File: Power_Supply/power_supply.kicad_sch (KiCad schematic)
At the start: 14 parts, among them J3 Conn_ARM_SWD_TagConnect, J6 Conn_01x04_Pin, SW1 SW_Push, U1 STM32F401RBTx, Y1 26MHz

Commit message: Updated Schematic and VIM878
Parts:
- removed J3: Conn_ARM_SWD_TagConnect, Connector:Tag-Connect_TC2030-IDC-NL_2x03_P1.27mm_Vertical, symbol Connector:Conn_ARM_SWD_TagConnect_TC2030-NL
- removed J6: Conn_01x04_Pin, symbol Connector:Conn_01x04_Pin
- removed JP1: Jumper_2_Open, TestPoint:TestPoint_Bridge_Pitch2.54mm_Drill0.7mm, symbol Jumper:Jumper_2_Open
- removed R1: 17K, symbol Device:R
- removed R6, R7, R8: 22, symbol Device:R
- added H1, H2, H3, H4: MountingHole, MountingHole:MountingHole_2.1mm, symbol Mechanical:MountingHole
- added H5, H6, H7, H8: MountingHole, MountingHole:MountingHole_3.2mm_M3, symbol Mechanical:MountingHole
- added J3: Conn_01x05_Pin, Connector_JST:JST_EH_B5B-EH-A_1x05_P2.50mm_Vertical, symbol Connector:Conn_01x05_Pin
- added J6: Conn_01x04_Socket, Connector_JST:JST_EH_B4B-EH-A_1x04_P2.50mm_Vertical, symbol Connector:Conn_01x04_Socket
- C11: footprint (none) -> Capacitor_SMD:C_0603_1608Metric
- C12: footprint (none) -> Capacitor_SMD:C_0402_1005Metric
- C14, C15: value 4pF -> 16pF; footprint (none) -> Capacitor_SMD:C_0402_1005Metric
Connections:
- net GND: now also U1.60 (BOOT0), J3.5 (Pin_5), J6.4 (Pin_4)
- net SCL: now also J6.3 (Pin_3)
- net SDA: now also J6.2 (Pin_2)
- net SWCLCK: now also J3.2 (Pin_2)
- net SWDIO: now also J3.3 (Pin_3)
- net SWO: now also J3.4 (Pin_4)
- net VDD: now also J3.1 (Pin_1), J6.1 (Pin_1); no longer U1.1 (VBAT), U1.19 (VDD), U1.32 (VDD), U1.48 (VDD), U1.64 (VDD)
- net SWD_RST: no longer names the net of C12.1, SW1.2, U1.7 (NRST)
- new net +3.3V: U1.1 (VBAT), U1.19 (VDD), U1.32 (VDD), U1.48 (VDD), U1.64 (VDD)

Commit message: Kicad model updated.
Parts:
- removed H7, H8: MountingHole, MountingHole:MountingHole_3.2mm_M3, symbol Mechanical:MountingHole
- J6: footprint Connector_JST:JST_EH_B4B-EH-A_1x04_P2.50mm_Vertical -> Connector_PinSocket_2.54mm:PinSocket_1x04_P2.54mm_Vertical
- Y1: footprint (none) -> Crystal:Crystal_SMD_ECS_CSM3X-2Pin_7.6x4.1mm
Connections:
- net VDD is gone; now on net +3.3V: J3.1 (Pin_1), J6.1 (Pin_1), U1.13 (VREF+)
- net Crystal_out: now reaches C15.2, U1.6 (PH1), Y1.1
- net Crystal_in: now reaches C14.2, U1.5 (PH0), Y1.2
- net V_Cap: now reaches C11.1, U1.30 (VCAP1)
- net Nrst: now reaches C12.1, SW1.2, U1.7 (NRST)
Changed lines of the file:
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@@
+    (stroke (width 0) (type default))
+  )
+  (wire (pts (xy 115.824 68.326) (xy 126.492 68.326))
     (stroke (width 0) (type default))
   )
@@
     (stroke (width 0) (type default))
   )
+  (wire (pts (xy 138.938 45.72) (xy 139.192 45.72))
+    (stroke (width 0) (type default))
+  )
   (wire (pts (xy 146.812 45.72) (xy 146.812 48.006))
     (stroke (width 0) (type default))
@@
     (stroke (width 0) (type default))
   )
-  (wire (pts (xy 139.192 42.926) (xy 139.192 45.72))
+  (wire (pts (xy 138.938 34.544) (xy 138.938 45.72))
     (stroke (width 0) (type default))
   )
@@
     (stroke (width 0) (type default))
   )
+  (wire (pts (xy 254.762 35.052) (xy 253.746 35.052))
+    (stroke (width 0) (type default))
+  )
   (wire (pts (xy 141.732 139.446) (xy 141.732 141.224))
     (stroke (width 0) (type default))
   )
-  (wire (pts (xy 126.492 68.326) (xy 115.824 68.326))
-    (stroke (width 0) (type default))
-  )
   (wire (pts (xy 141.732 48.006) (xy 141.732 45.72))
     (stroke (width 0) (type default))
@@
     (fill (type none))
   )
-  (rectangle (start 240.792 99.822) (end 283.718 143.002)
+  (rectangle (start 240.792 99.822) (end 283.718 130.556)
     (stroke (width 0) (type default))
     (fill (type none))
@@
   (text "Components\n" (at 52.324 65.786 90)
     (effects (font (size 2 2)) (justify left bottom))
+  )
+  (label "V_Cap" (at 114.3 124.206 0) (fields_autoplaced)
+    (effects (font (size 1.27 1.27)) (justify left bottom))
+  )
+  (label "Crystal_out" (at 116.332 70.866 0) (fields_autoplaced)
+    (effects (font (size 1.27 1.27)) (justify left bottom))
+  )
+  (label "Nrst" (at 117.094 53.086 0) (fields_autoplaced)
+    (effects (font (size 1.27 1.27)) (justify left bottom))
+  )
+  (label "Crystal_in" (at 116.332 68.326 0) (fields_autoplaced)
+    (effects (font (size 1.27 1.27)) (justify left bottom))
   )
   (global_label "SWCLCK" (shape input) (at 253.746 37.592 0) (fields_autoplaced)
@@
     )
   )
-  (global_label "VDD" (shape input) (at 260.604 75.946 180) (fields_autoplaced)
-    (effects (font (size 1.27 1.27)) (justify right))
-    (property "Intersheetrefs" "${INTERSHEET_REFS}" (at 254.0696 75.946 0)
-      (effects (font (size 1.27 1.27)) (justify right) hide)
-    )
-  )
   (global_label "SWDIO" (shape input) (at 253.746 40.132 0) (fields_autoplaced)
     (effects (font (size 1.27 1.27)) (justify left))
@@
     )
   )
-  (global_label "VDD" (shape input) (at 122.682 63.246 180) (fields_autoplaced)
-    (effects (font (size 1.27 1.27)) (justify right))
-    (property "Intersheetrefs" "${INTERSHEET_REFS}" (at 116.1476 63.246 0)
-      (effects (font (size 1.27 1.27)) (justify right) hide)
-    )
-  )
-  (global_label "VDD" (shape input) (at 253.746 35.052 0) (fields_autoplaced)
-    (effects (font (size 1.27 1.27)) (justify left))
-    (property "Intersheetrefs" "${INTERSHEET_REFS}" (at 260.2804 35.052 0)
-      (effects (font (size 1.27 1.27)) (justify left) hide)
-    )
-  )
   (global_label "SWCLCK" (shape input) (at 159.385 88.519 0) (fields_autoplaced)
     (effects (font (size 1.27 1.27)) (justify left))
@@
     )
   )
-  (symbol (lib_id "Mechanical:MountingHole") (at 244.348 133.858 0) (unit 1)
-    (in_bom yes) (on_board yes) (dnp no) (fields_autoplaced)
-    (property "Reference" "H7" (at 246.888 133.223 0)
-      (effects (font (size 1.27 1.27)) (justify left))
-    )
-    (property "Value" "MountingHole" (at 246.888 135.763 0)
-      (effects (font (size 1.27 1.27)) (justify left))
-    )
-    (property "Footprint" "MountingHole:MountingHole_3.2mm_M3" (at 244.348 133.858 0)
-      (effects (font (size 1.27 1.27)) hide)
-    )
-    (property "Datasheet" "~" (at 244.348 133.858 0)
-      (effects (font (size 1.27 1.27)) hide)
-    )
-    (instances
-      (project "power_supply"
-        (path "/82b2e9f2-0f9f-45f5-b878-35b85461c206"
-          (reference "H7") (unit 1)
-        )
-      )
-    )
-  )
   (symbol (lib_id "power:GND") (at 120.904 58.166 270) (unit 1)
     (in_bom yes) (on_board yes) (dnp no)
@@
       (effects (font (size 1.27 1.27)) (justify left))
     )
-    (property "Footprint" "Connector_JST:JST_EH_B4B-EH-A_1x04_P2.50mm_Vertical" (at 267.97 78.486 0)
+    (property "Footprint" "Connector_PinSocket_2.54mm:PinSocket_1x04_P2.54mm_Vertical" (at 267.97 78.486 0)
       (effects (font (size 1.27 1.27)) hide)
     )
@@
       (effects (font (size 1.27 1.27)) (justify right))
     )
-    (property "Footprint" "" (at 110.744 69.596 0)
+    (property "Footprint" "Crystal:Crystal_SMD_ECS_CSM3X-2Pin_7.6x4.1mm" (at 110.744 69.596 0)
       (effects (font (size 1.27 1.27)) hide)
     )
@@
         (path "/82b2e9f2-0f9f-45f5-b878-35b85461c206"
           (reference "C11") (unit 1)
+        )
+      )
+    )
+  )
+  (symbol (lib_id "power:+3.3V") (at 260.604 75.946 90) (unit 1)
+    (in_bom yes) (on_board yes) (dnp no)
+    (property "Reference" "#PWR017" (at 264.414 75.946 0)
+      (effects (font (size 1.27 1.27)) hide)
+    )
+    (property "Value" "+3.3V" (at 256.794 75.438 90)
+      (effects (font (size 1.27 1.27)) (justify left))
+    )
+    (property "Footprint" "" (at 260.604 75.946 0)
+      (effects (font (size 1.27 1.27)) hide)
+    )
+    (property "Datasheet" "" (at 260.604 75.946 0)
+      (effects (font (size 1.27 1.27)) hide)
+    )
+    (pin "1")
+    (instances
+      (project "power_supply"
+        (path "/82b2e9f2-0f9f-45f5-b878-35b85461c206"
+          (reference "#PWR017") (unit 1)
         )
       )
@@
     )
   )
+  (symbol (lib_id "power:+3.3V") (at 122.682 63.246 90) (unit 1)
+    (in_bom yes) (on_board yes) (dnp no)
+    (property "Reference" "#PWR015" (at 126.492 63.246 0)
+      (effects (font (size 1.27 1.27)) hide)
+    )
+    (property "Value" "+3.3V" (at 117.348 66.04 0)
+      (effects (font (size 1.27 1.27)) (justify left))
+    )
+    (property "Footprint" "" (at 122.682 63.246 0)
+      (effects (font (size 1.27 1.27)) hide)
+    )
+    (property "Datasheet" "" (at 122.682 63.246 0)
+      (effects (font (size 1.27 1.27)) hide)
+    )
+    (pin "1")
+    (instances
+      (project "power_supply"
+        (path "/82b2e9f2-0f9f-45f5-b878-35b85461c206"
+          (reference "#PWR015") (unit 1)
+        )
+      )
+    )
+  )
   (symbol (lib_id "Mechanical:MountingHole") (at 266.954 125.222 0) (unit 1)
     (in_bom yes) (on_board yes) (dnp no) (fields_autoplaced)
@@
     )
   )
-  (symbol (lib_id "power:+3.3V") (at 139.192 42.926 0) (unit 1)
-    (in_bom yes) (on_board yes) (dnp no) (fields_autoplaced)
-    (property "Reference" "#PWR038" (at 139.192 46.736 0)
-      (effects (font (size 1.27 1.27)) hide)
-    )
-    (property "Value" "+3.3V" (at 139.192 39.37 0)
-      (effects (font (size 1.27 1.27)))
-    )
-    (property "Footprint" "" (at 139.192 42.926 0)
-      (effects (font (size 1.27 1.27)) hide)
-    )
-    (property "Datasheet" "" (at 139.192 42.926 0)
+  (symbol (lib_id "power:+3.3V") (at 138.938 34.544 0) (unit 1)
+    (in_bom yes) (on_board yes) (dnp no) (fields_autoplaced)
+    (property "Reference" "#PWR038" (at 138.938 38.354 0)
+      (effects (font (size 1.27 1.27)) hide)
+    )
+    (property "Value" "+3.3V" (at 138.938 30.988 0)
+      (effects (font (size 1.27 1.27)))
+    )
+    (property "Footprint" "" (at 138.938 34.544 0)
+      (effects (font (size 1.27 1.27)) hide)
+    )
+    (property "Datasheet" "" (at 138.938 34.544 0)
       (effects (font (size 1.27 1.27)) hide)
     )
@@
         (path "/82b2e9f2-0f9f-45f5-b878-35b85461c206"
           (reference "C15") (unit 1)
+        )
+      )
+    )
+  )
+  (symbol (lib_id "power:+3.3V") (at 254.762 35.052 270) (unit 1)
+    (in_bom yes) (on_board yes) (dnp no)
+    (property "Reference" "#PWR018" (at 250.952 35.052 0)
+      (effects (font (size 1.27 1.27)) hide)
+    )
+    (property "Value" "+3.3V" (at 258.572 35.56 90)
+      (effects (font (size 1.27 1.27)) (justify left))
+    )
+    (property "Footprint" "" (at 254.762 35.052 0)
+      (effects (font (size 1.27 1.27)) hide)
+    )
+    (property "Datasheet" "" (at 254.762 35.052 0)
+      (effects (font (size 1.27 1.27)) hide)
+    )
+    (pin "1")
+    (instances
+      (project "power_supply"
+        (path "/82b2e9f2-0f9f-45f5-b878-35b85461c206"
+          (reference "#PWR018") (unit 1)
         )
       )
@@
         )
       )
-    )
-  )
-  (symbol (lib_id "Mechanical:MountingHole") (at 267.208 134.366 0) (unit 1)
-    (in_bom yes) (on_board yes) (dnp no) (fields_autoplaced)
-    (property "Reference" "H8" (at 269.748 133.731 0)
-      (effects (font (size 1.27 1.27)) (justify left))
-    )
-    (property "Value" "MountingHole" (at 269.748 136.271 0)
-      (effects (font (size 1.27 1.27)) (justify left))
-    )
-    (property "Footprint" "MountingHole:MountingHole_3.2mm_M3" (at 267.208 134.366 0)
-      (effects (font (size 1.27 1.27)) hide)
-    )
-    (property "Datasheet" "~" (at 267.208 134.366 0)
-      (effects (font (size 1.27 1.27)) hide)
-    )
-    (instances
-      (project "power_supply"
-        (path "/82b2e9f2-0f9f-45f5-b878-35b85461c206"
-          (reference "H8") (unit 1)
-        )
-      )

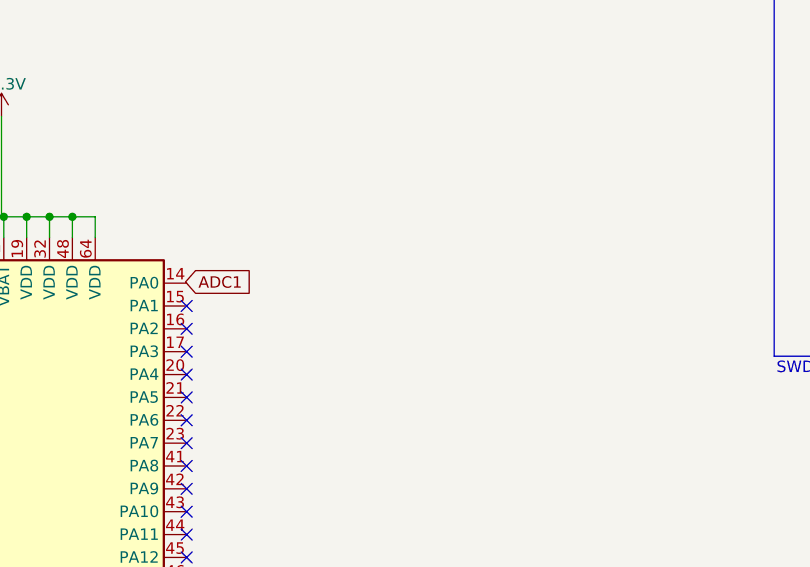
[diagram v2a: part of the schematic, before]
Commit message: Updated schematics. and added the correct Driver files for stm32f401
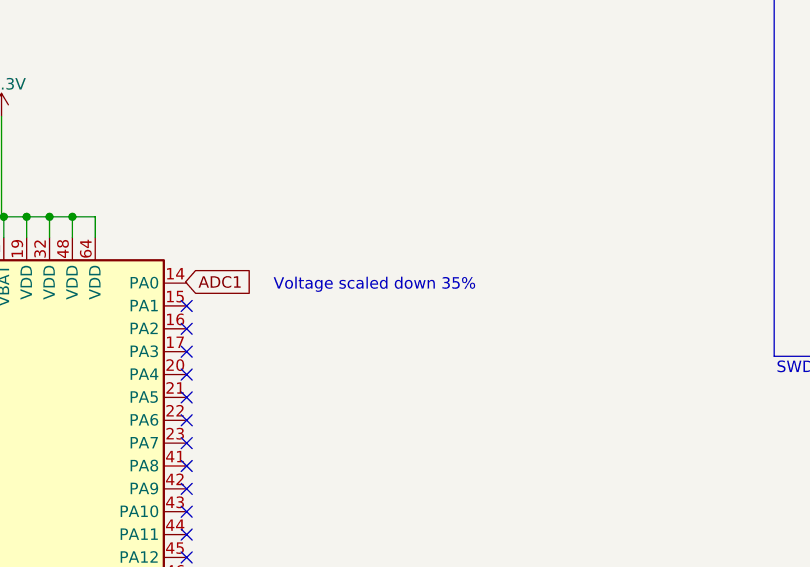
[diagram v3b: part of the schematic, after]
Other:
- note added: "Voltage scaled down 35%"
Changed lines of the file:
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@@
+    (effects (font (size 1.27 1.27)) (justify left bottom))
+  )
+  (text "Voltage scaled down 35%\n" (at 169.164 54.102 0)
     (effects (font (size 1.27 1.27)) (justify left bottom))
   )
